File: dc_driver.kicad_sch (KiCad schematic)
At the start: 0 parts

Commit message: DC motor drivers added
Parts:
- added C21, C22, C23, C24, C25, C26, C27, C28: 47u 16V, Capacitor_SMD:CP_Elec_5x5.3, symbol Device:C_Polarized_Small
- added D2, D3, D4, D5: D_Zener_Small, Diode_SMD:D_SMC, symbol Device:D_Zener_Small
- added J1, J10, J12, J13, J14, J15, J17, J18, J19, J20, J3, J4, J5, J7, J8, J9: Conn_01x02, Connector_PinHeader_1.00mm:PinHeader_1x02_P1.00mm_Vertical, symbol Connector_Generic:Conn_01x02
- added J11, J16, J2, J6: Conn_01x02, symbol Connector_Generic:Conn_01x02
- added R13, R14, R15, R16: 220, Resistor_SMD:R_0805_2012Metric, symbol Device:R_Small
- added U4, U5, U6, U7: MX1508, MX1508:SOIC127P600X177-16N, symbol MX1508:MX1508
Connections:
- new net: J15.1 (Pin_1), U6.12 (OUTA2)
- new net: J15.2 (Pin_2), U6.9 (OUTB2)
- new net: J10.1 (Pin_1), U5.12 (OUTA2)
- new net: J10.2 (Pin_2), U5.9 (OUTB2)
- new net: J20.1 (Pin_1), U7.12 (OUTA2)
- new net: J20.2 (Pin_2), U7.9 (OUTB2)
- new net: J7.1 (Pin_1), U5.3 (INB1)
- new net: J7.2 (Pin_2), U5.2 (INA1)
- new net: J4.1 (Pin_1), U4.3 (INB1)
- new net: J4.2 (Pin_2), U4.2 (INA1)
- new net: J17.1 (Pin_1), U7.3 (INB1)
- new net: J17.2 (Pin_2), U7.2 (INA1)
- new net: J5.1 (Pin_1), U4.7 (INB2)
- new net: J5.2 (Pin_2), U4.6 (INA2)
- new net: J3.2 (Pin_2), U4.13 (OUTB1)
- new net: J3.1 (Pin_1), U4.16 (OUTA1)
- new net: J12.1 (Pin_1), U6.3 (INB1)
- new net: J12.2 (Pin_2), U6.2 (INA1)
- new net: J13.1 (Pin_1), U6.7 (INB2)
- new net: J13.2 (Pin_2), U6.6 (INA2)
- new net: J1.1 (Pin_1), U4.12 (OUTA2)
- new net: J1.2 (Pin_2), U4.9 (OUTB2)
- new net: J19.1 (Pin_1), U7.16 (OUTA1)
- new net: J19.2 (Pin_2), U7.13 (OUTB1)
- new net: J8.2 (Pin_2), U5.6 (INA2)
- new net: J8.1 (Pin_1), U5.7 (INB2)
- new net: J14.2 (Pin_2), U6.13 (OUTB1)
- new net: J14.1 (Pin_1), U6.16 (OUTA1)
- new net: J18.2 (Pin_2), U7.6 (INA2)
- new net: J18.1 (Pin_1), U7.7 (INB2)
- new net: J9.2 (Pin_2), U5.13 (OUTB1)
- new net: J9.1 (Pin_1), U5.16 (OUTA1)
- new net 5V: C21.2, C22.1, C22.2, C23.2, C24.1, C24.2, C25.2, C26.1, C26.2, C27.2, C28.1, C28.2, D2.1 (K), D2.2 (A), D3.1 (K), D3.2 (A), D4.1 (K), D4.2 (A), D5.1 (K), D5.2 (A), J11.1 (Pin_1), J16.1 (Pin_1), J2.1 (Pin_1), J6.1 (Pin_1), R13.2, R14.2, R15.2, R16.2, U4.1 (VCC1), U4.4 (VDD1), U4.5 (VCC2), U4.8 (VDD2), U5.1 (VCC1), U5.4 (VDD1), U5.5 (VCC2), U5.8 (VDD2), U6.1 (VCC1), U6.4 (VDD1), U6.5 (VCC2), U6.8 (VDD2), U7.1 (VCC1), U7.4 (VDD1), U7.5 (VCC2), U7.8 (VDD2)
- new net GND: U4.10 (AGND2), U4.11 (PGND2), U4.14 (AGND1), U4.15 (PGND1), U5.10 (AGND2), U5.11 (PGND2), U5.14 (AGND1), U5.15 (PGND1), U6.10 (AGND2), U6.11 (PGND2), U6.14 (AGND1), U6.15 (PGND1), U7.10 (AGND2), U7.11 (PGND2), U7.14 (AGND1), U7.15 (PGND1)
- new net VCC: C21.1, C23.1, C25.1, C27.1, J11.2 (Pin_2), J16.2 (Pin_2), J2.2 (Pin_2), J6.2 (Pin_2), R13.1, R14.1, R15.1, R16.1

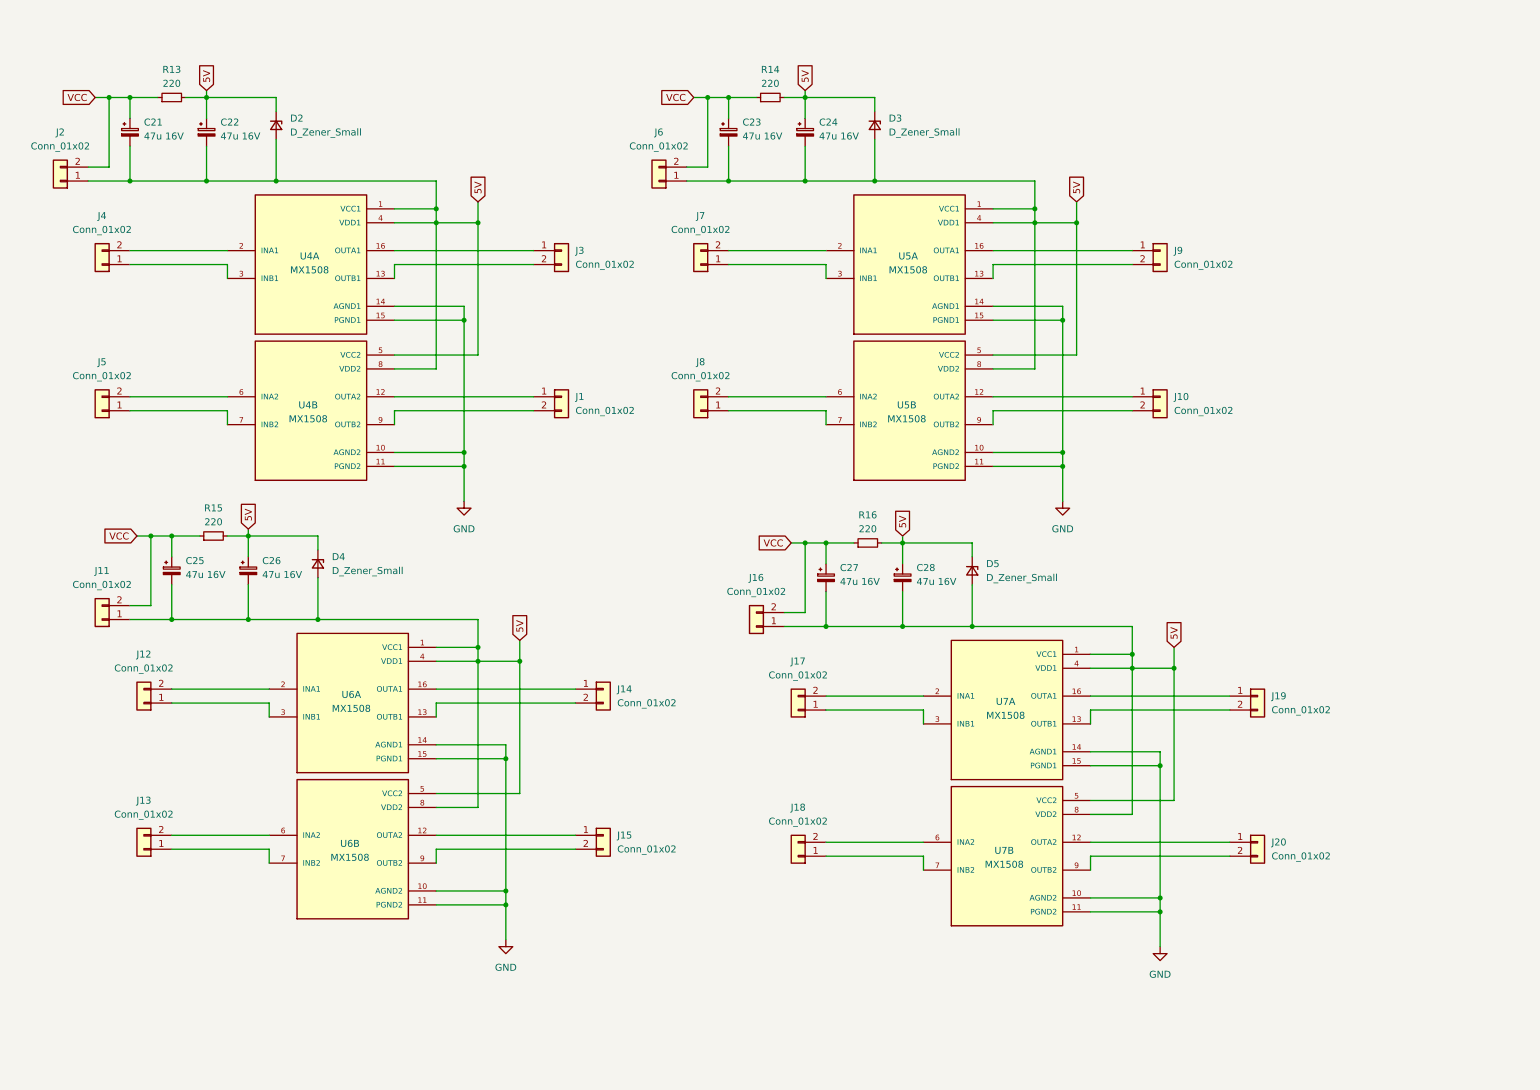
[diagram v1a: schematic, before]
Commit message: DC motor zener rev.
Zener diode value in dc motor was changed to BZV55 5.1V
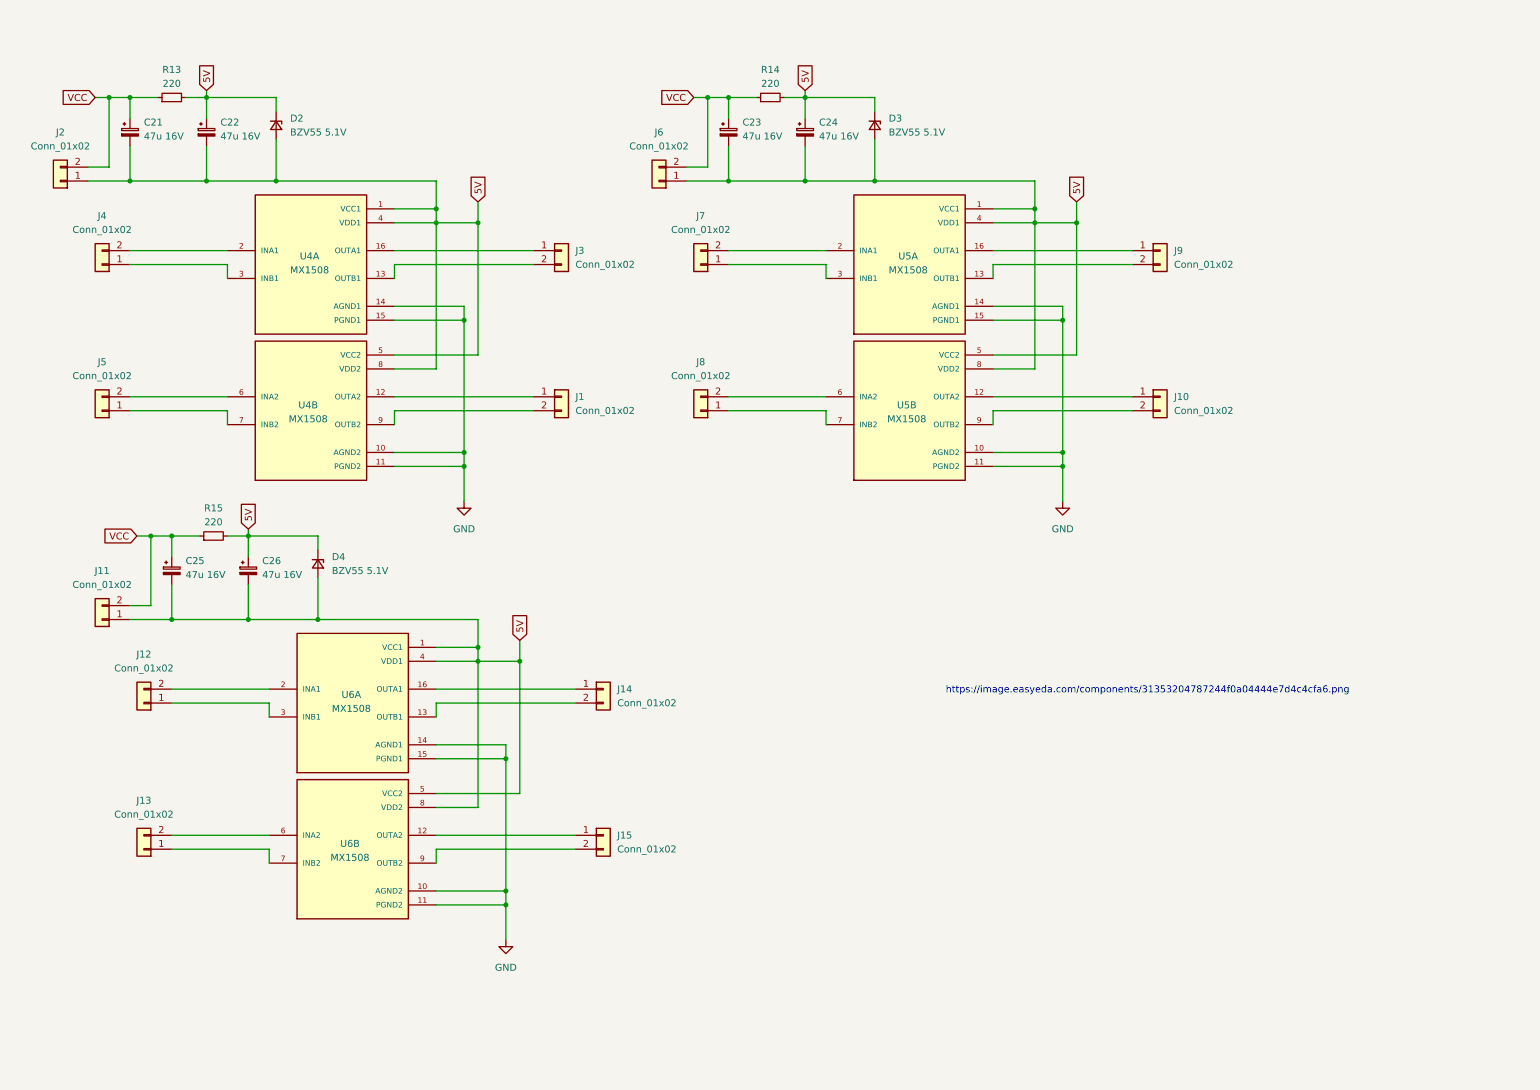
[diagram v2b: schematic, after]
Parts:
- removed C27, C28: 47u 16V, Capacitor_SMD:CP_Elec_5x5.3, symbol Device:C_Polarized_Small
- removed D5: D_Zener_Small, Diode_SMD:D_SMC, symbol Device:D_Zener_Small
- removed J16: Conn_01x02, symbol Connector_Generic:Conn_01x02
- removed J17, J18, J19, J20: Conn_01x02, Connector_PinHeader_1.00mm:PinHeader_1x02_P1.00mm_Vertical, symbol Connector_Generic:Conn_01x02
- removed R16: 220, Resistor_SMD:R_0805_2012Metric, symbol Device:R_Small
- removed U7: MX1508, MX1508:SOIC127P600X177-16N, symbol MX1508:MX1508
- D2, D3, D4: value D_Zener_Small -> BZV55 5.1V
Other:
- note added: "https://image.easyeda.com/components/31353204787244f0a04444e7d4c4cfa6.png"

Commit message: stm32 added
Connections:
- net 5V: no longer C21.2, C22.2, C23.2, C24.2, C25.2, C26.2, D2.2 (A), D3.2 (A), D4.2 (A), J11.1 (Pin_1), J2.1 (Pin_1), J6.1 (Pin_1), U6.5 (VCC2), U6.8 (VDD2)
- new net: C25.2, C26.2, D4.2 (A), J11.1 (Pin_1)
- new net: C23.2, C24.2, D3.2 (A), J6.1 (Pin_1)
- new net: C21.2, C22.2, D2.2 (A), J2.1 (Pin_1)
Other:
- note added: "GPIO ile sürülecek bunlar 5V çalışıyo sıkıntı?"
- moved on the sheet: J1, J10, J14, J15, J3, J9

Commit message: DC motor driver revised
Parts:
- removed C21, C23, C25: 47u 16V, Capacitor_SMD:CP_Elec_5x5.3, symbol Device:C_Polarized_Small
- removed D2, D3, D4: BZV55 5.1V, Diode_SMD:D_SMC, symbol Device:D_Zener_Small
- removed J11, J2, J6: Conn_01x02, symbol Connector_Generic:Conn_01x02
- removed J12, J3, J7: Conn_01x02, Connector_PinHeader_1.00mm:PinHeader_1x02_P1.00mm_Vertical, symbol Connector_Generic:Conn_01x02
- removed R13, R14, R15: 220, Resistor_SMD:R_0805_2012Metric, symbol Device:R_Small
- removed U4, U5, U6: MX1508, MX1508:SOIC127P600X177-16N, symbol MX1508:MX1508
- added D10, D11, D12, D13, D14, D15, D16, D17, D18, D19, D2, D20, D21, D22, D23, D24, D25, D3, D4, D5, D6, D7, D8, D9: SS34-DO214AB-HT, Diode_SMD:D_SMC, symbol Device:D_Small
- added J12, J2, J7: Conn_01x04, symbol Connector_Generic:Conn_01x04
- added U1, U6, U9: L298N, Package_TO_SOT_THT:TO-220-15_P2.54x2.54mm_StaggerOdd_Lead4.58mm_Vertical, symbol Driver_Motor:L298N
- C22, C24: value 47u 16V -> 220uF 35V; footprint Capacitor_SMD:CP_Elec_5x5.3 -> Capacitor_SMD:CP_Elec_8x10.5
- C26: value 47u 16V -> 220uF 35V; footprint Capacitor_SMD:CP_Elec_5x5.3 -> (none)
- J1, J10, J13, J14, J15, J4, J5, J8, J9: footprint Connector_PinHeader_1.00mm:PinHeader_1x02_P1.00mm_Vertical -> (none)
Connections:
- net GND: now also C22.2, C24.2, C26.2, D11.2 (A), D13.2 (A), D15.2 (A), D17.2 (A), D19.2 (A), D21.2 (A), D23.2 (A), D25.2 (A), D6.2 (A), D7.2 (A), D8.2 (A), D9.2 (A), U1.1 (SENSE_A), U1.15 (SENSE_B), U1.8 (GND), U6.1 (SENSE_A), U6.15 (SENSE_B), U6.8 (GND), U9.1 (SENSE_A), U9.15 (SENSE_B), U9.8 (GND)
- net at J15.1 (Pin_1): now also D22.2 (A), D23.1 (K), U9.13 (OUT3)
- net at J15.2 (Pin_2): now also D24.2 (A), D25.1 (K), U9.14 (OUT4)
- net at J10.1 (Pin_1): now also D14.2 (A), D15.1 (K), U6.13 (OUT3)
- net at J10.2 (Pin_2): now also D16.2 (A), D17.1 (K), U6.14 (OUT4)
- net at J4.1 (Pin_1): now also D2.2 (A), D6.1 (K), U1.2 (OUT1)
- net at J4.2 (Pin_2): now also D3.2 (A), D7.1 (K), U1.3 (OUT2)
- net at J5.1 (Pin_1): now also D4.2 (A), D8.1 (K), U1.13 (OUT3)
- net at J5.2 (Pin_2): now also D5.2 (A), D9.1 (K), U1.14 (OUT4)
- net at J13.1 (Pin_1): now also U9.11 (EnB)
- net at J13.2 (Pin_2): now also U9.6 (EnA)
- net at J1.1 (Pin_1): now also U1.11 (EnB)
- net at J1.2 (Pin_2): now also U1.6 (EnA)
- net at J8.2 (Pin_2): now also U6.6 (EnA)
- net at J8.1 (Pin_1): now also U6.11 (EnB)
- net at J14.2 (Pin_2): now also D20.2 (A), D21.1 (K), U9.3 (OUT2)
- net at J14.1 (Pin_1): now also D18.2 (A), D19.1 (K), U9.2 (OUT1)
- net at J9.2 (Pin_2): now also D12.2 (A), D13.1 (K), U6.3 (OUT2)
- net at J9.1 (Pin_1): now also D10.2 (A), D11.1 (K), U6.2 (OUT1)
- removed net 5V: C22.1, C24.1, C26.1
- new net: J2.2 (Pin_2), U1.10 (IN3)
- new net: J2.1 (Pin_1), U1.12 (IN4)
- new net: C22.1, D2.1 (K), D3.1 (K), D4.1 (K), D5.1 (K), U1.4 (Vs)
- new net: J2.4 (Pin_4), U1.5 (IN1)
- new net: J2.3 (Pin_3), U1.7 (IN2)
- new net: C26.1, D18.1 (K), D20.1 (K), D22.1 (K), D24.1 (K), U9.4 (Vs)
- new net: J7.2 (Pin_2), U6.10 (IN3)
- new net: J7.1 (Pin_1), U6.12 (IN4)
- new net: C24.1, D10.1 (K), D12.1 (K), D14.1 (K), D16.1 (K), U6.4 (Vs)
- new net: J7.4 (Pin_4), U6.5 (IN1)
- new net: J7.3 (Pin_3), U6.7 (IN2)
- new net: J12.2 (Pin_2), U9.10 (IN3)
- new net: J12.1 (Pin_1), U9.12 (IN4)
- new net: J12.4 (Pin_4), U9.5 (IN1)
- new net: J12.3 (Pin_3), U9.7 (IN2)
- new net 3V3: U1.9 (Vss), U6.9 (Vss), U9.9 (Vss)
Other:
- note added: "https://image.easyeda.com/components/d43d3c46faff4ba8b6a4d30e04717420.png"
- note added: "https://www.handsontec.com/dataspecs/L298N%20Motor%20Driver.pdf"
- note removed: "GPIO ile sürülecek bunlar 5V çalışıyo sıkıntı?"
- note removed: "https://image.easyeda.com/components/31353204787244f0a04444e7d4c4cfa6.png"

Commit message: DC motor driver revised
l298n Vss->5v
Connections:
- net 3V3 renamed 5V1
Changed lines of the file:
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@@
 		)
 	)
-	(global_label "3V3"
-		(shape input)
-		(at 54.61 114.3 90)
-		(fields_autoplaced yes)
-		(effects
-			(font
-				(size 1.27 1.27)
-			)
-			(justify left)
-		)
-		(property "Intersheetrefs" "${INTERSHEET_REFS}"
-			(at 54.61 107.8072 90)
-			(effects
-				(font
-					(size 1.27 1.27)
-				)
-				(justify left)
-				(hide yes)
-			)
-		)
-	)
-	(global_label "3V3"
+	(global_label "5V1"
 		(shape input)
 		(at 165.1 27.94 90)
@@
 		)
 	)
-	(global_label "3V3"
+	(global_label "5V1"
 		(shape input)
 		(at 50.8 29.21 90)
@@
 			(effects
 				(font
+					(size 1.27 1.27)
+				)
+				(justify left)
+				(hide yes)
+			)
+		)
+	)
+	(global_label "5V1"
+		(shape input)
+		(at 54.61 114.3 90)
+		(fields_autoplaced yes)
+		(effects
+			(font
+				(size 1.27 1.27)
+			)
+			(justify left)
+		)
+		(property "Intersheetrefs" "${INTERSHEET_REFS}"
+			(at 54.61 107.8072 90)
+			(effects
+				(font

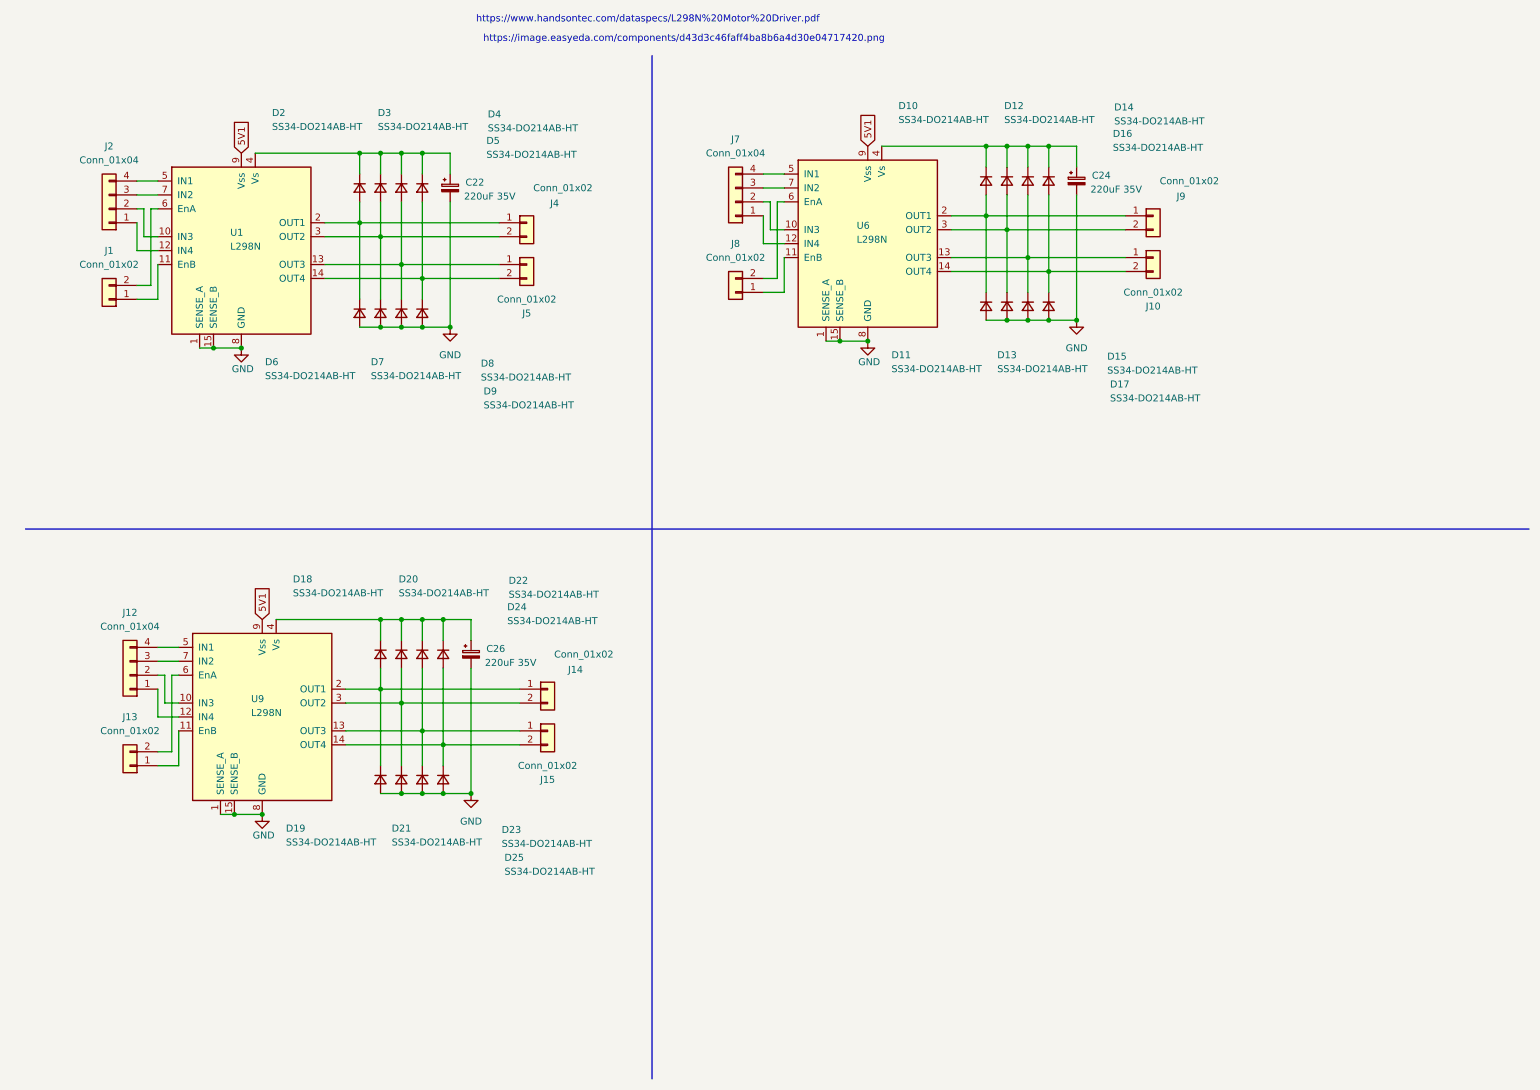
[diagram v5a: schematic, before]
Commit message: added components
servo controller, esp32
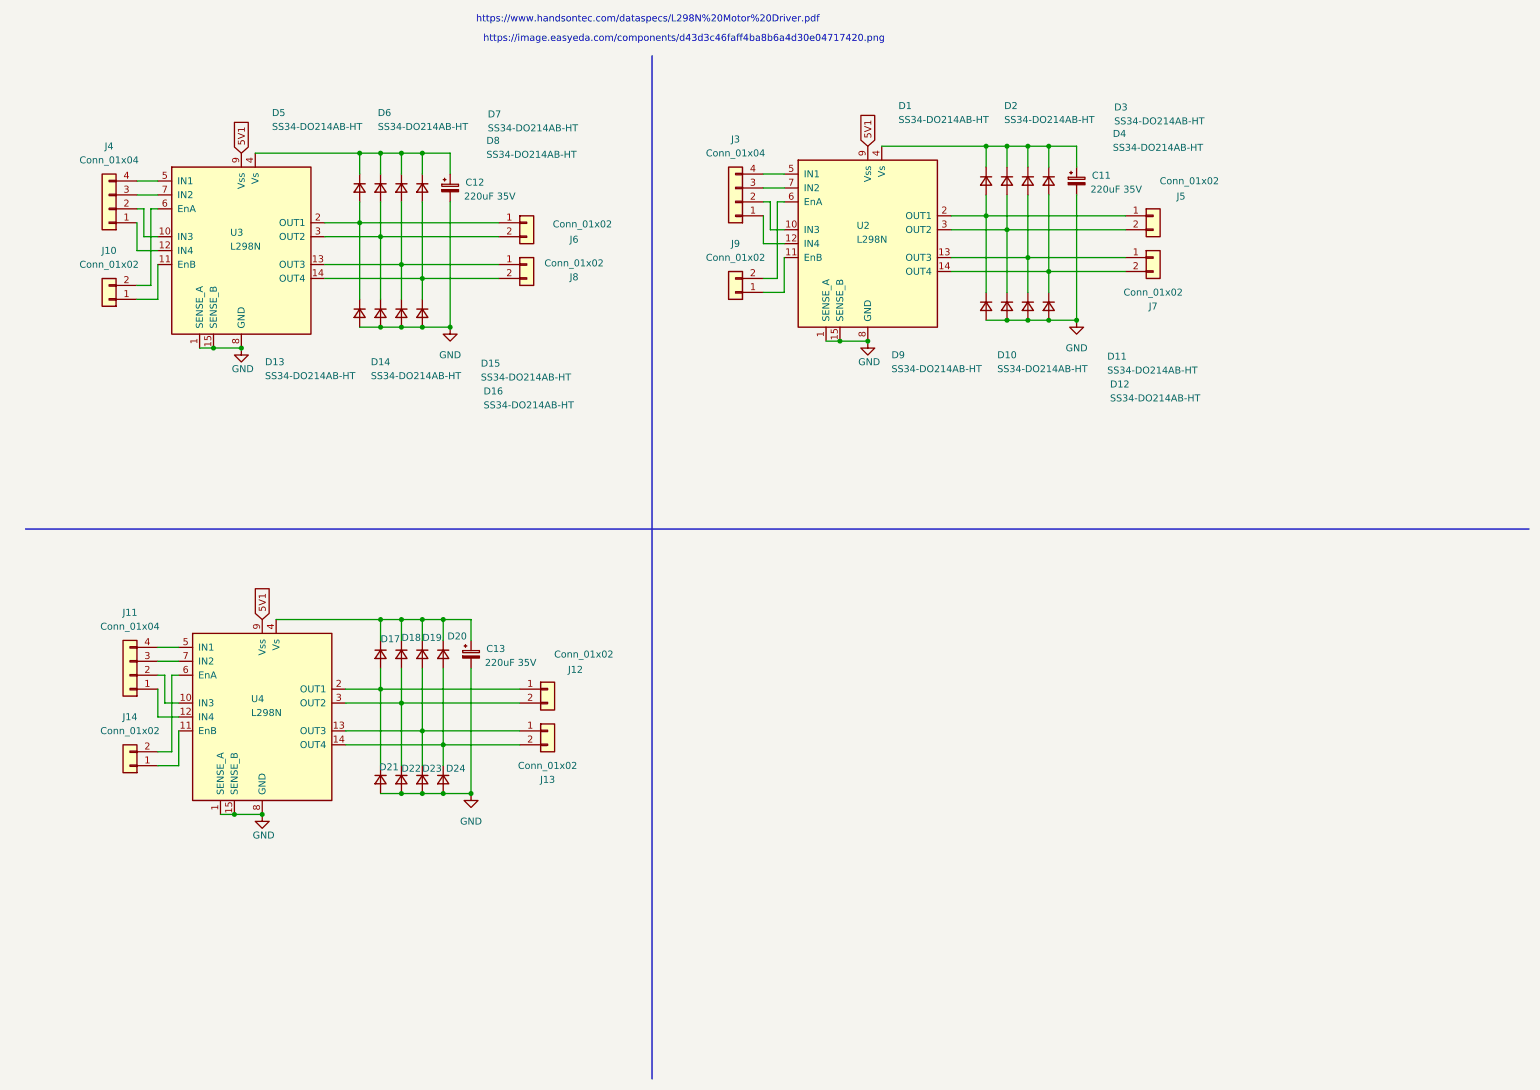
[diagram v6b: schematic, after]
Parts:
- renumbered C24 to C11, C22 to C12, C26 to C13, D10 to D1, D13 to D10, D15 to D11, D17 to D12, D6 to D13, D7 to D14, D8 to D15, D9 to D16, D18 to D17, D20 to D18, D22 to D19, D12 to D2, D24 to D20, D19 to D21, D21 to D22, D25 to D24, D14 to D3, D16 to D4, D2 to D5, D3 to D6, D4 to D7, D5 to D8, D11 to D9, J1 to J10, J12 to J11, J14 to J12, J15 to J13, J13 to J14, J7 to J3, J2 to J4, J9 to J5, J4 to J6, J10 to J7, J5 to J8, J8 to J9, U6 to U2, U1 to U3, U9 to U4
